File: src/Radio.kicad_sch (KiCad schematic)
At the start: 11 parts

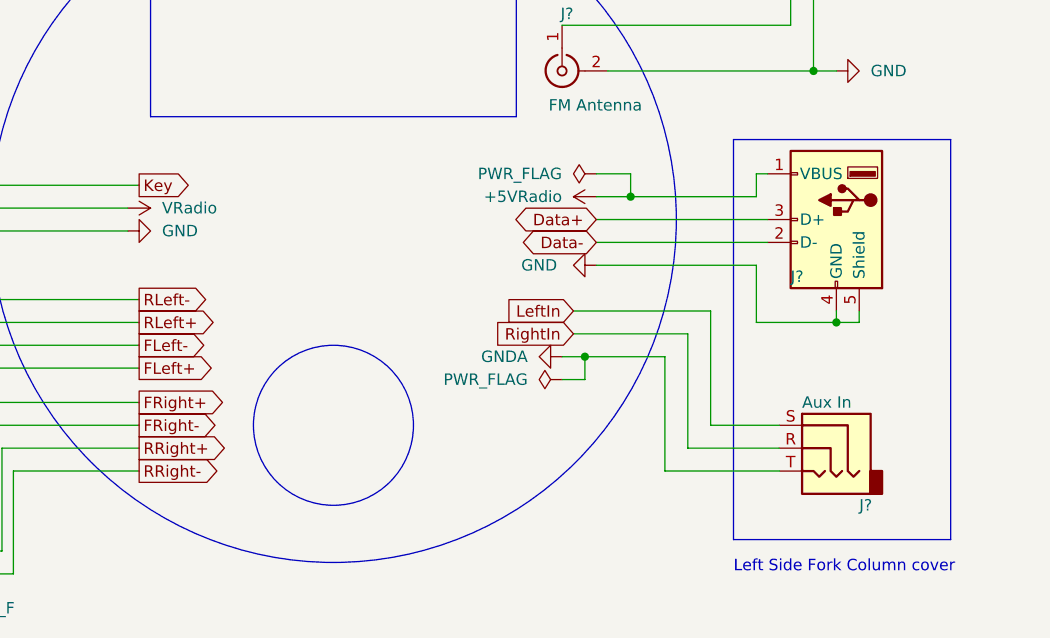
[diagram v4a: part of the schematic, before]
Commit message: simplify circuit diagram. Remove unecessary features; Split board into two components|
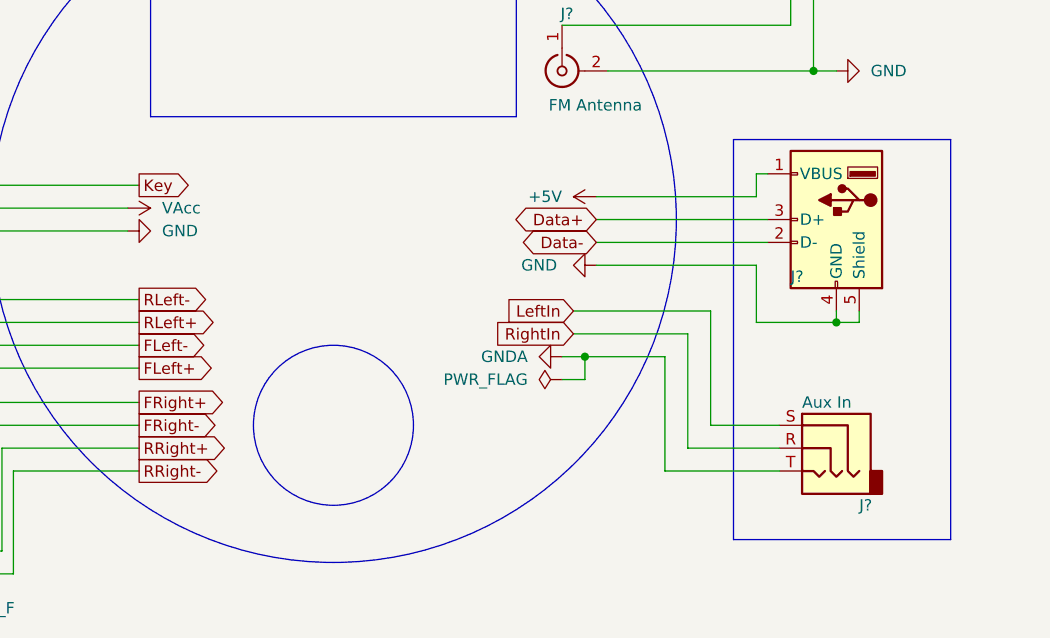
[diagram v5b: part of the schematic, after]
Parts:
- J? (x2): footprint Connector_Molex:Molex_Mini-Fit_Jr_5566-08A_2x04_P4.20mm_Vertical -> (none)
- J?: footprint Connector_Molex:Molex_Mini-Fit_Jr_5566-04A_2x02_P4.20mm_Vertical -> (none)
- J?: footprint Connector_USB:USB_A_Molex_67643_Horizontal -> (none)
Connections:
- net +5VRadio renamed +5V
- net VRadio renamed VAcc
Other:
- note removed: "Left Side Fork Column cover"
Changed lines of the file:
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@@
   (title_block
     (title "Velex VX163 Radio")
-    (comment 1 "Wire gauge: 1mm² / 18AWG")
-    (comment 3 "Labels at the cable harness are in reference to each connected component")
-    (comment 4 "Labels are in reference to the local I/O scope boxes")
+    (comment 4 "Wire gauge: 1mm² / 18AWG")
   )
   (junction (at 54.61 76.2) (diameter 0) (color 0 0 0 0)
@@
   (junction (at 227.33 115.57) (diameter 0) (color 0 0 0 0)
   )
-  (junction (at 232.41 97.79) (diameter 0) (color 0 0 0 0)
-  )
   (no_connect (at 142.24 67.31))
-  (wire (pts (xy 232.41 95.25) (xy 232.41 97.79))
-    (stroke (width 0) (type default))
-  )
   (wire (pts (xy 252.73 74.93) (xy 252.73 83.82))
     (stroke (width 0) (type default))
@@
     (stroke (width 0) (type default))
   )
-  (wire (pts (xy 232.41 97.79) (xy 246.38 97.79))
-    (stroke (width 0) (type default))
-  )
   (wire (pts (xy 82.55 102.87) (xy 97.79 102.87))
     (stroke (width 0) (type default))
@@
     (stroke (width 0) (type default))
   )
-  (wire (pts (xy 228.6 95.25) (xy 232.41 95.25))
-    (stroke (width 0) (type default))
-  )
   (wire (pts (xy 57.15 72.39) (xy 57.15 76.2))
     (stroke (width 0) (type default))
@@
     (stroke (width 0) (type default))
   )
-  (wire (pts (xy 228.6 97.79) (xy 232.41 97.79))
+  (wire (pts (xy 228.6 97.79) (xy 246.38 97.79))
     (stroke (width 0) (type default))
   )
@@
   )
   (text "Handlebar speakers" (at 67.31 71.12 0)
-    (effects (font (size 1.27 1.27)) (justify left bottom))
-  )
-  (text "Left Side Fork Column cover" (at 243.84 139.7 0)
     (effects (font (size 1.27 1.27)) (justify left bottom))
   )
@@
       (effects (font (size 1.27 1.27)) (justify left))
     )
-    (property "Footprint" "Connector_Molex:Molex_Mini-Fit_Jr_5566-08A_2x04_P4.20mm_Vertical" (at 152.4 134.62 0)
+    (property "Footprint" "" (at 152.4 134.62 0)
       (effects (font (size 1.27 1.27)) hide)
     )
@@
         )
         (path "/e63e39d7-6ac0-4ffd-8aa3-1841a4541b55/ddab4412-d22a-447e-a3b8-944a9a68a530"
-          (reference "J47") (unit 1)
+          (reference "J22") (unit 1)
         )
       )
@@
         )
         (path "/e63e39d7-6ac0-4ffd-8aa3-1841a4541b55/ddab4412-d22a-447e-a3b8-944a9a68a530"
-          (reference "J49") (unit 1)
+          (reference "J24") (unit 1)
         )
       )
@@
         )
         (path "/e63e39d7-6ac0-4ffd-8aa3-1841a4541b55/ddab4412-d22a-447e-a3b8-944a9a68a530"
-          (reference "#PWR070") (unit 1)
-        )
-      )
-    )
-  )
-  (symbol (lib_id "power:PWR_FLAG") (at 228.6 95.25 90) (unit 1)
-    (in_bom yes) (on_board yes) (dnp no)
-    (property "Reference" "#FLG?" (at 226.695 95.25 0)
-      (effects (font (size 1.27 1.27)) hide)
-    )
-    (property "Value" "PWR_FLAG" (at 224.79 95.25 90)
+          (reference "#PWR051") (unit 1)
+        )
+      )
+    )
+  )
+  (symbol (lib_id "Local Components:VAcc") (at 176.53 99.06 270) (unit 1)
+    (in_bom yes) (on_board yes) (dnp no)
+    (property "Reference" "#PWR?" (at 172.72 99.06 0)
+      (effects (font (size 1.27 1.27)) hide)
+    )
+    (property "Value" "VAcc" (at 180.34 99.06 90)
       (effects (font (size 1.27 1.27)) (justify left))
     )
-    (property "Footprint" "" (at 228.6 95.25 0)
-      (effects (font (size 1.27 1.27)) hide)
-    )
-    (property "Datasheet" "~" (at 228.6 95.25 0)
+    (property "Footprint" "" (at 176.53 99.06 0)
+      (effects (font (size 1.27 1.27)) hide)
+    )
+    (property "Datasheet" "" (at 176.53 99.06 0)
       (effects (font (size 1.27 1.27)) hide)
     )
@@
       (project "dragstar-infotainment"
         (path "/e63e39d7-6ac0-4ffd-8aa3-1841a4541b55/5d40715c-dfc9-4b95-9cc7-adbd4b609d9b"
-          (reference "#FLG?") (unit 1)
-        )
-        (path "/e63e39d7-6ac0-4ffd-8aa3-1841a4541b55/ddab4412-d22a-447e-a3b8-944a9a68a530"
-          (reference "#FLG011") (unit 1)
+          (reference "#PWR?") (unit 1)
+        )
+        (path "/e63e39d7-6ac0-4ffd-8aa3-1841a4541b55/ddab4412-d22a-447e-a3b8-944a9a68a530"
+          (reference "#PWR047") (unit 1)
         )
       )
@@
       (effects (font (size 1.27 1.27)) (justify left))
     )
-    (property "Footprint" "Connector_Molex:Molex_Mini-Fit_Jr_5566-08A_2x04_P4.20mm_Vertical" (at 74.93 100.33 0)
+    (property "Footprint" "" (at 74.93 100.33 0)
       (effects (font (size 1.27 1.27)) hide)
     )
@@
         )
         (path "/e63e39d7-6ac0-4ffd-8aa3-1841a4541b55/ddab4412-d22a-447e-a3b8-944a9a68a530"
-          (reference "J45") (unit 1)
+          (reference "J20") (unit 1)
         )
       )
@@
         )
         (path "/e63e39d7-6ac0-4ffd-8aa3-1841a4541b55/ddab4412-d22a-447e-a3b8-944a9a68a530"
-          (reference "J48") (unit 1)
+          (reference "J23") (unit 1)
         )
       )
@@
         )
         (path "/e63e39d7-6ac0-4ffd-8aa3-1841a4541b55/ddab4412-d22a-447e-a3b8-944a9a68a530"
-          (reference "#PWR071") (unit 1)
+          (reference "#PWR052") (unit 1)
         )
       )
@@
     )
   )
-  (symbol (lib_id "Local Components:+5VRadio") (at 228.6 97.79 90) (unit 1)
-    (in_bom yes) (on_board yes) (dnp no)
-    (property "Reference" "#PWR069" (at 232.41 97.79 0)
-      (effects (font (size 1.27 1.27)) hide)
-    )
-    (property "Value" "+5VRadio" (at 224.79 97.79 90)
+  (symbol (lib_id "power:+5V") (at 228.6 97.79 90) (unit 1)
+    (in_bom yes) (on_board yes) (dnp no)
+    (property "Reference" "#PWR050" (at 232.41 97.79 0)
+      (effects (font (size 1.27 1.27)) hide)
+    )
+    (property "Value" "+5V" (at 224.79 97.79 90)
       (effects (font (size 1.27 1.27)) (justify left))
     )
@@
       (project "dragstar-infotainment"
         (path "/e63e39d7-6ac0-4ffd-8aa3-1841a4541b55/ddab4412-d22a-447e-a3b8-944a9a68a530"
-          (reference "#PWR069") (unit 1)
+          (reference "#PWR050") (unit 1)
         )
       )
@@
       (effects (font (size 1.27 1.27)) (justify right))
     )
-    (property "Footprint" "Connector_Molex:Molex_Mini-Fit_Jr_5566-04A_2x02_P4.20mm_Vertical" (at 149.86 69.85 0)
+    (property "Footprint" "" (at 149.86 69.85 0)
       (effects (font (size 1.27 1.27)) hide)
     )
@@
         )
         (path "/e63e39d7-6ac0-4ffd-8aa3-1841a4541b55/ddab4412-d22a-447e-a3b8-944a9a68a530"
-          (reference "J46") (unit 1)
+          (reference "J21") (unit 1)
         )
       )
@@
         )
         (path "/e63e39d7-6ac0-4ffd-8aa3-1841a4541b55/ddab4412-d22a-447e-a3b8-944a9a68a530"
-          (reference "#PWR068") (unit 1)
+          (reference "#PWR049") (unit 1)
         )
       )
@@
       (effects (font (size 1.27 1.27)) (justify right) hide)
     )
-    (property "Footprint" "Connector_USB:USB_A_Molex_67643_Horizontal" (at 251.46 101.6 0)
+    (property "Footprint" "" (at 251.46 101.6 0)
       (effects (font (size 1.27 1.27)) hide)
     )
@@
         )
         (path "/e63e39d7-6ac0-4ffd-8aa3-1841a4541b55/ddab4412-d22a-447e-a3b8-944a9a68a530"
-          (reference "J50") (unit 1)
+          (reference "J25") (unit 1)
         )
       )
@@
   (symbol (lib_id "power:GND") (at 176.53 101.6 90) (unit 1)
     (in_bom yes) (on_board yes) (dnp no)
-    (property "Reference" "#PWR067" (at 182.88 101.6 0)
+    (property "Reference" "#PWR048" (at 182.88 101.6 0)
       (effects (font (size 1.27 1.27)) hide)
     )
@@
       (project "dragstar-infotainment"
         (path "/e63e39d7-6ac0-4ffd-8aa3-1841a4541b55/ddab4412-d22a-447e-a3b8-944a9a68a530"
-          (reference "#PWR067") (unit 1)
+          (reference "#PWR048") (unit 1)
         )
       )
@@
         )
       )
-    )
-  )
-  (symbol (lib_id "Local Components:VRadio") (at 176.53 99.06 270) (unit 1)
-    (in_bom yes) (on_board yes) (dnp no)
-    (property "Reference" "#PWR?" (at 172.72 99.06 0)
-      (effects (font (size 1.27 1.27)) hide)
-    )
-    (property "Value" "VRadio" (at 180.34 99.06 90)
-      (effects (font (size 1.27 1.27)) (justify left))
-    )
-    (property "Footprint" "" (at 176.53 99.06 0)
-      (effects (font (size 1.27 1.27)) hide)
-    )
-    (property "Datasheet" "" (at 176.53 99.06 0)
-      (effects (font (size 1.27 1.27)) hide)
-    )
-    (pin "1")
-    (instances
-      (project "dragstar-infotainment"
-        (path "/e63e39d7-6ac0-4ffd-8aa3-1841a4541b55"
-          (reference "#PWR?") (unit 1)
-        )
-        (path "/e63e39d7-6ac0-4ffd-8aa3-1841a4541b55/ddab4412-d22a-447e-a3b8-944a9a68a530"
-          (reference "#PWR066") (unit 1)
-        )
-      )

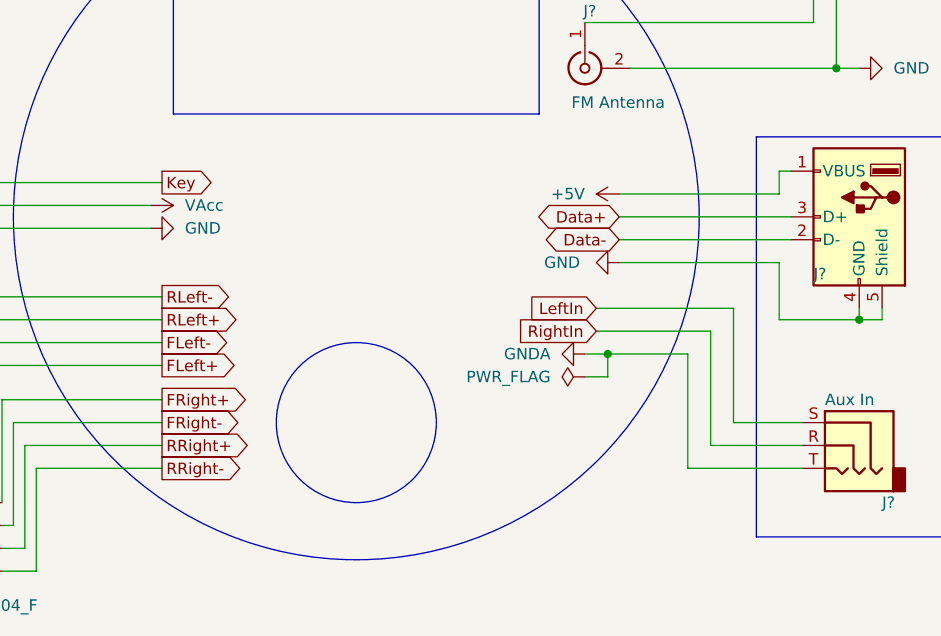
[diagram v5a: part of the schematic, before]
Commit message: Simplify circuit diagram. Remove unecessary features
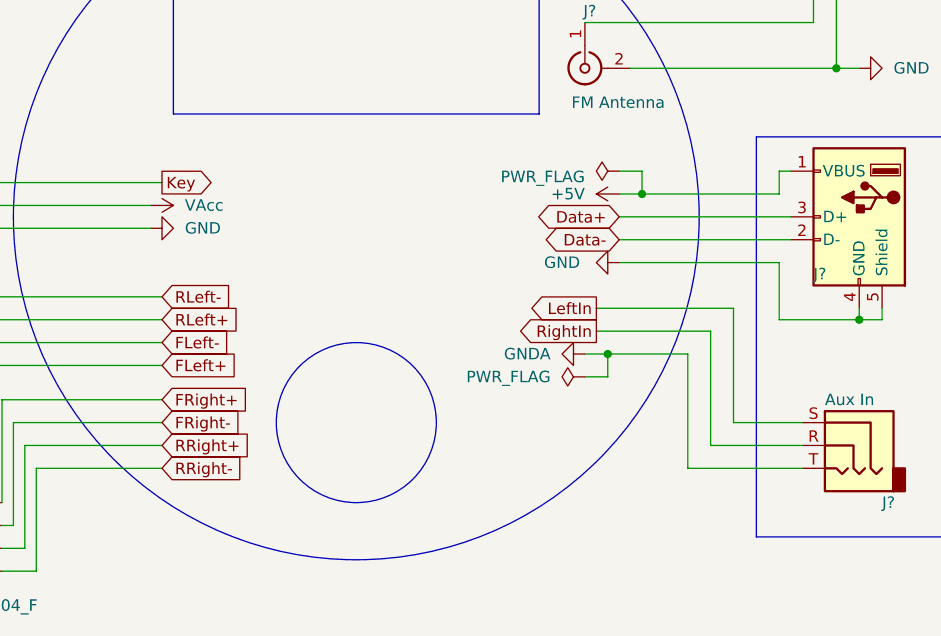
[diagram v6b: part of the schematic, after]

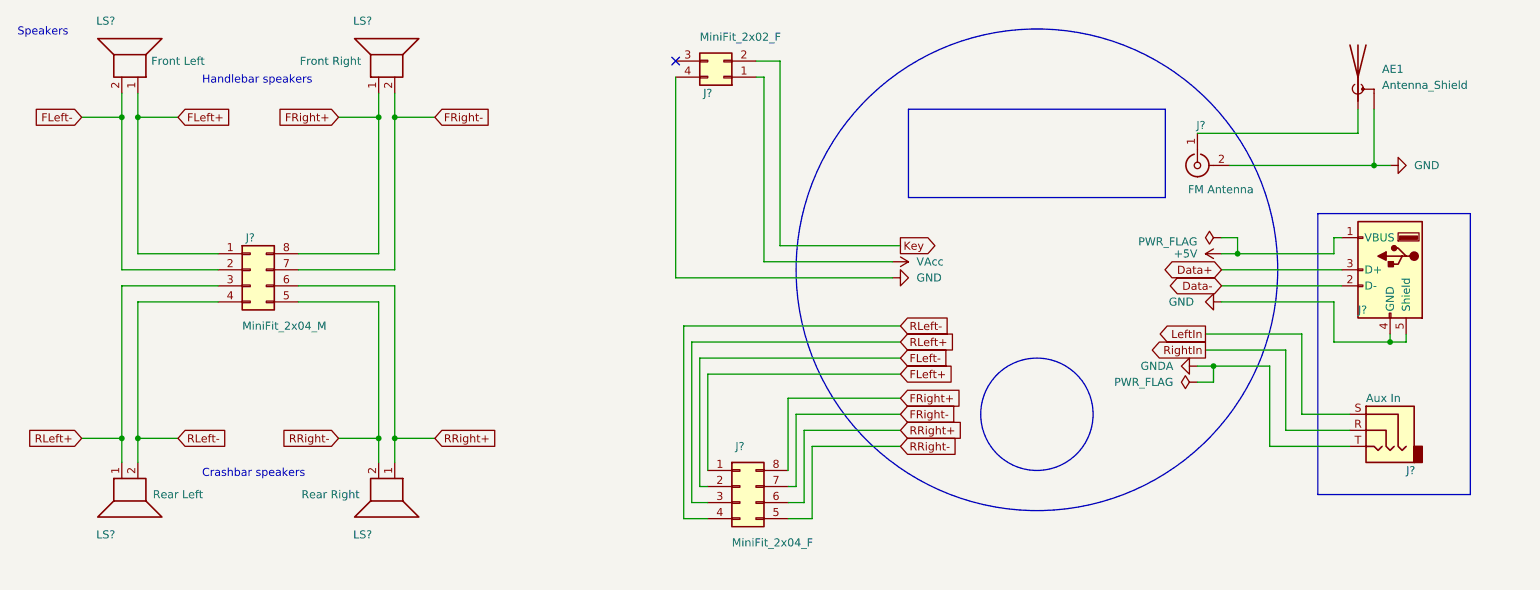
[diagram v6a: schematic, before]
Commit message: Fix battery sensor
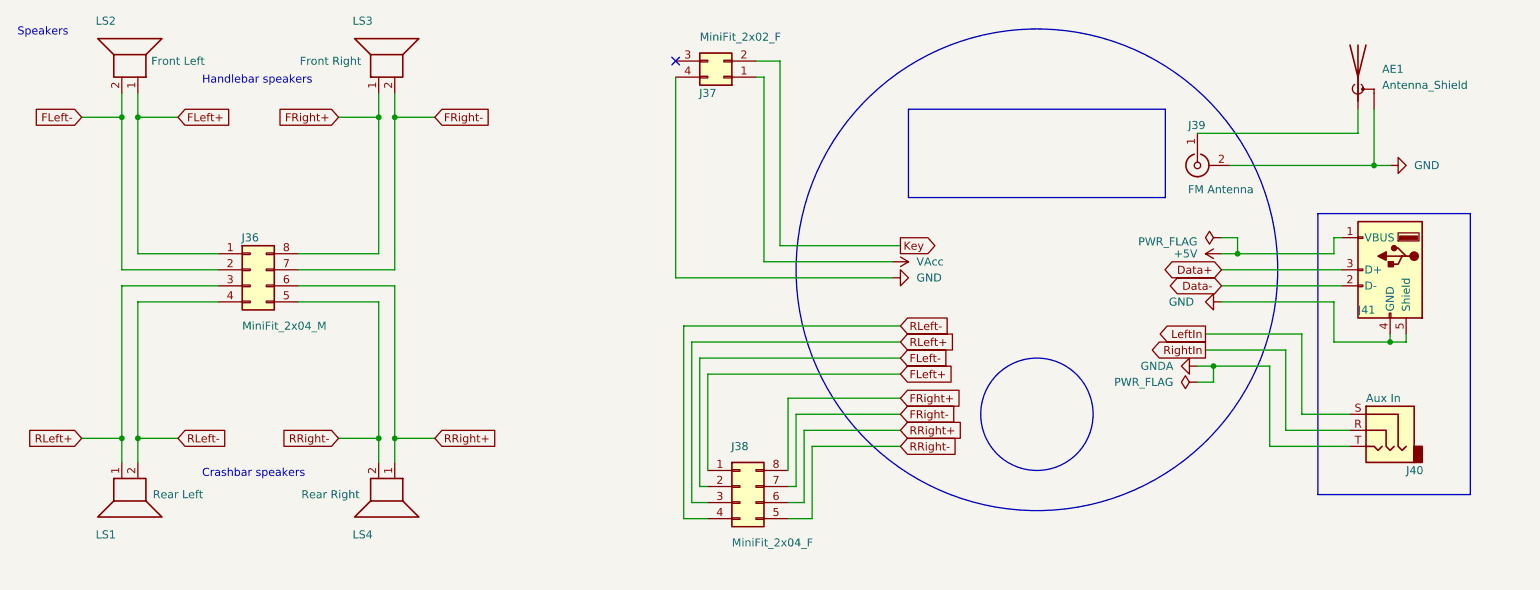
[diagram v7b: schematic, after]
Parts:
- gave numbers to parts that had none: 10
